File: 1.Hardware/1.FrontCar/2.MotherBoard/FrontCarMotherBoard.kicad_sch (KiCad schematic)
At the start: 0 parts

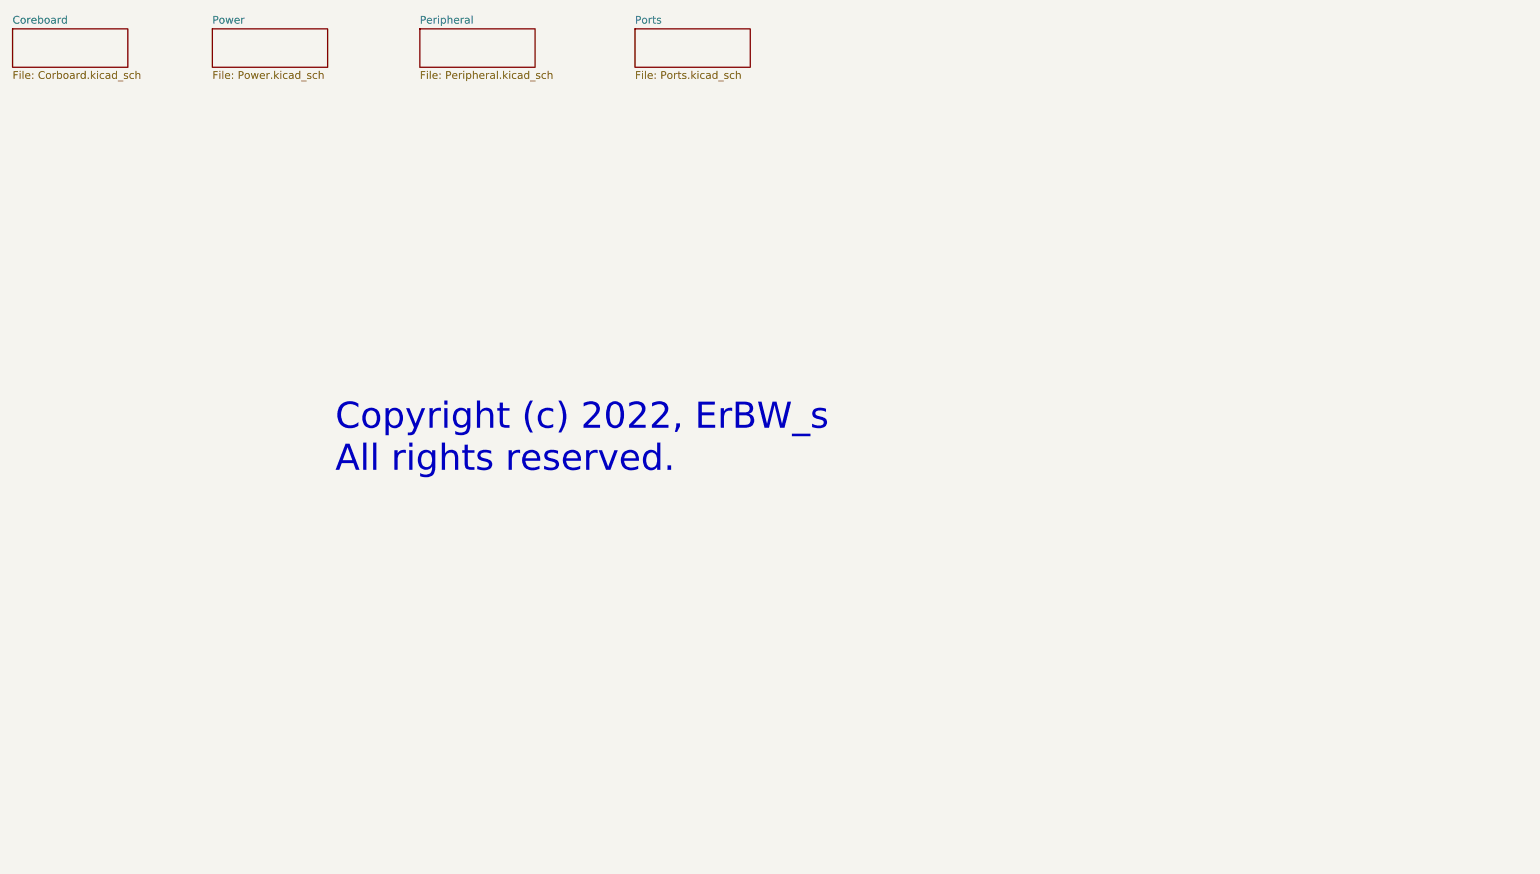
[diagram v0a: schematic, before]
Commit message: 母板原理图完成
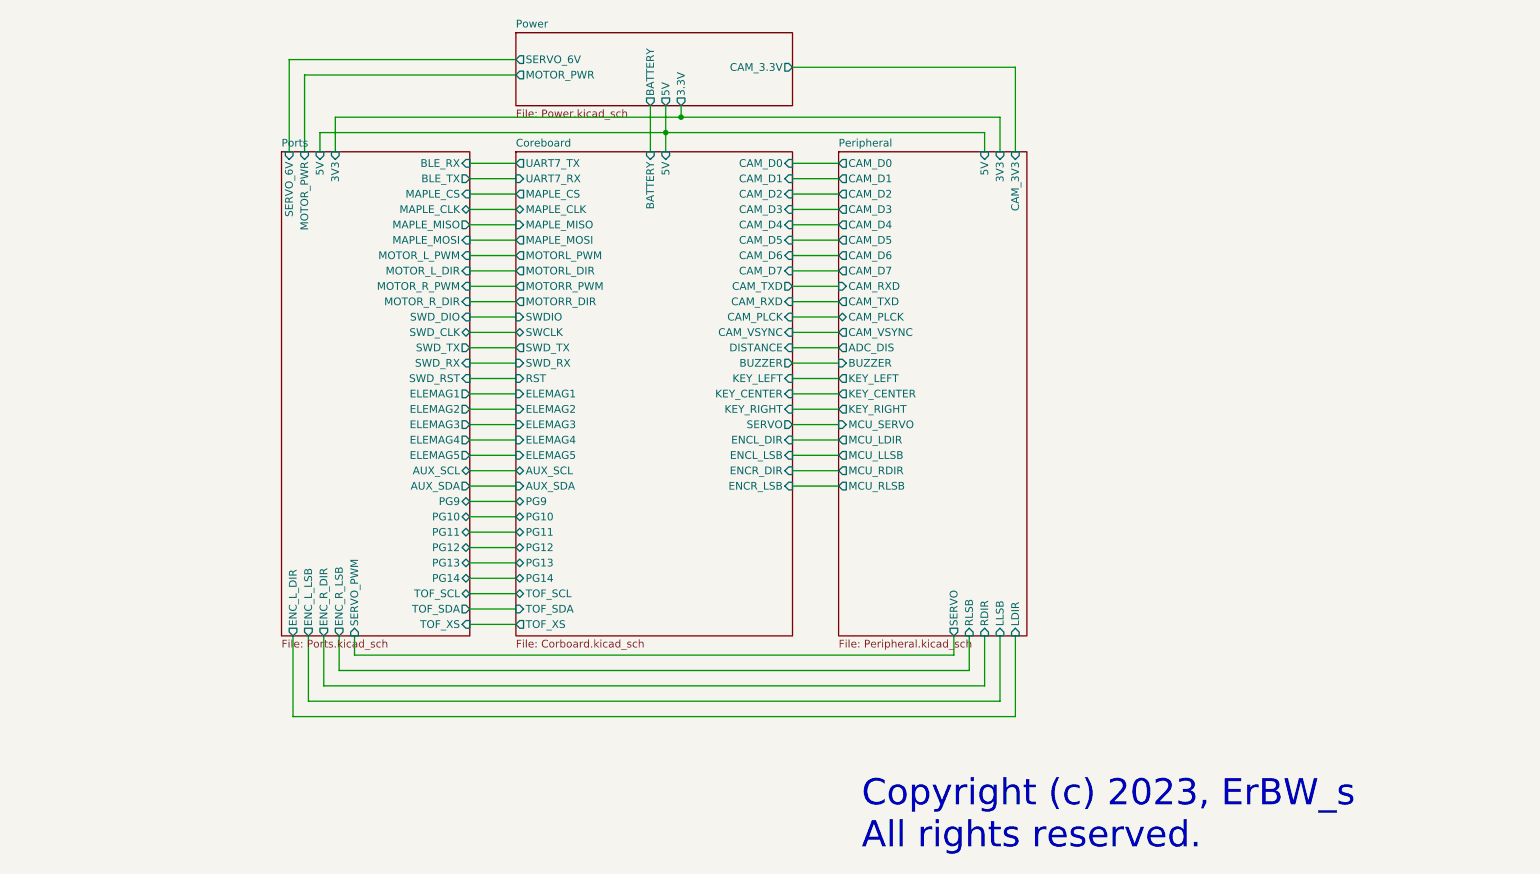
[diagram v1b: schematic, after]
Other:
- sheet Coreboard ports: added 5V, AUX_SCL, AUX_SDA, BATTERY, BUZZER, CAM_D0, CAM_D1, CAM_D2, CAM_D3, CAM_D4, CAM_D5, CAM_D6, CAM_D7, CAM_PLCK, CAM_RXD, CAM_TXD, CAM_VSYNC, DISTANCE, ELEMAG1, ELEMAG2, ELEMAG3, ELEMAG4, ELEMAG5, ENCL_DIR, ENCL_LSB, ENCR_DIR, ENCR_LSB, KEY_CENTER, KEY_LEFT, KEY_RIGHT, MAPLE_CLK, MAPLE_CS, MAPLE_MISO, MAPLE_MOSI, MOTORL_DIR, MOTORL_PWM, MOTORR_DIR, MOTORR_PWM, PG10, PG11, PG12, PG13, PG14, PG9, RST, SERVO, SWCLK, SWDIO, SWD_RX, SWD_TX, TOF_SCL, TOF_SDA, TOF_XS, UART7_RX, UART7_TX; removed none
- sheet Peripheral ports: added 3V3, 5V, ADC_DIS, BUZZER, CAM_3V3, CAM_D0, CAM_D1, CAM_D2, CAM_D3, CAM_D4, CAM_D5, CAM_D6, CAM_D7, CAM_PLCK, CAM_RXD, CAM_TXD, CAM_VSYNC, KEY_CENTER, KEY_LEFT, KEY_RIGHT, LDIR, LLSB, MCU_LDIR, MCU_LLSB, MCU_RDIR, MCU_RLSB, MCU_SERVO, RDIR, RLSB, SERVO; removed none
- sheet Ports ports: added 3V3, 5V, AUX_SCL, AUX_SDA, BLE_RX, BLE_TX, ELEMAG1, ELEMAG2, ELEMAG3, ELEMAG4, ELEMAG5, ENC_L_DIR, ENC_L_LSB, ENC_R_DIR, ENC_R_LSB, MAPLE_CLK, MAPLE_CS, MAPLE_MISO, MAPLE_MOSI, MOTOR_L_DIR, MOTOR_L_PWM, MOTOR_PWR, MOTOR_R_DIR, MOTOR_R_PWM, PG10, PG11, PG12, PG13, PG14, PG9, SERVO_6V, SERVO_PWM, SWD_CLK, SWD_DIO, SWD_RST, SWD_RX, SWD_TX, TOF_SCL, TOF_SDA, TOF_XS; removed none
- sheet Power ports: added 3.3V, 5V, BATTERY, CAM_3.3V, MOTOR_PWR, SERVO_6V; removed none
- note added: "Copyright (c) 2023, ErBW_s All rights reserved."
- note removed: "Copyright (c) 2022, ErBW_s All rights reserved."

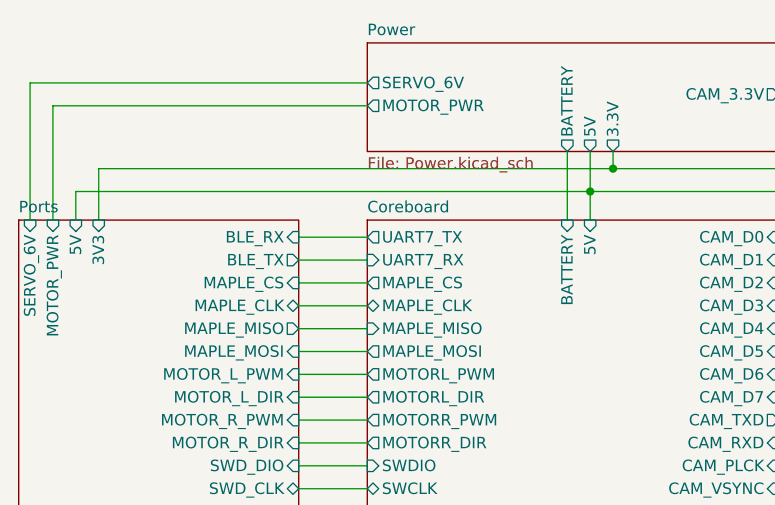
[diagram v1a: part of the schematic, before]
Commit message: 更新母板原理图封装
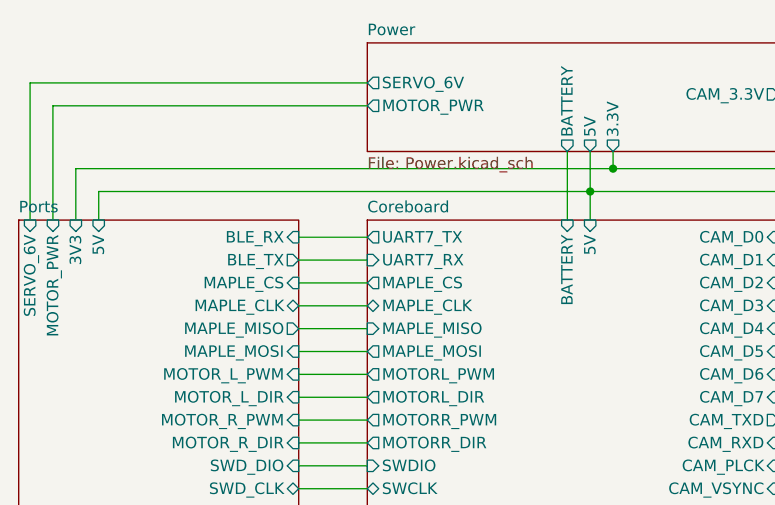
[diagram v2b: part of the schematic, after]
